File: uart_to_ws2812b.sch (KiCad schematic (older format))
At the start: 27 parts, among them J1 USB_B_Micro, J2 Prog. Header, J3 Power Header, J4 UART, J5 I2C, J6 SPI, J8 Conn_01x03, J9 Conn_01x03, Q1 Q_NPN_BEC, SW1 SW_Push

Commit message: Updated copper pours to avoid short between V_USB and GND
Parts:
- Q1: Mfr Part # (none) -> MMBT3904; Supplier (none) -> LCSC; Supplier Part # (none) -> C181119
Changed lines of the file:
@@
 F 2 "Package_TO_SOT_SMD:SOT-23" H 5450 3700 50  0001 C CNN
 F 3 "~" H 5250 3600 50  0001 C CNN
+F 4 "MMBT3904" H 5250 3600 50  0001 C CNN "Mfr Part #"
+F 5 "LCSC" H 5250 3600 50  0001 C CNN "Supplier"
+F 6 "C181119" H 5250 3600 50  0001 C CNN "Supplier Part #"
 	1    5250 3600
 	1    0    0    -1

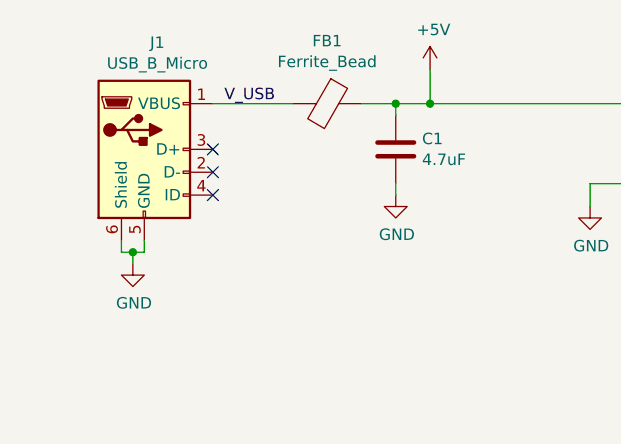
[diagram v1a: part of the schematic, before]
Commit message: Shorted D+ and D- to indicate charging mode
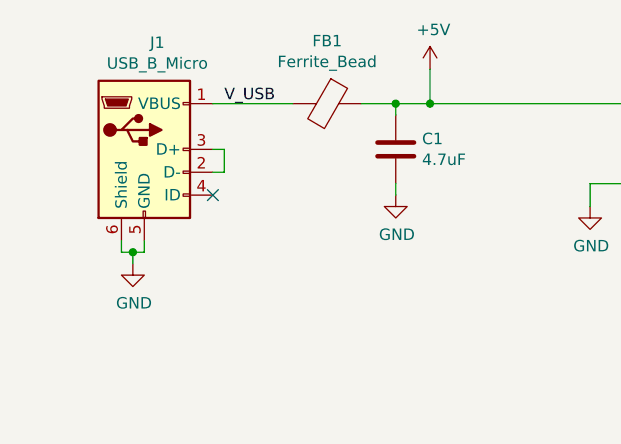
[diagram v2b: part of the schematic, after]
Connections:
- net at J1.2 (D-): now also J1.3 (D+)
- no-connect marks 4 -> 2

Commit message: Changed to a level shifting IC for the LED data logic
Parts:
- removed Q1: Q_NPN_BEC, Package_TO_SOT_SMD:SOT-23, symbol Device:Q_NPN_BEC
- removed R1: 1kR, Resistor_SMD:R_0603_1608Metric, symbol Device:R
- removed R2, R3: 10kR, Resistor_SMD:R_0603_1608Metric, symbol Device:R
- added C2, C22: 0.1uF, Capacitor_SMD:C_0603_1608Metric, symbol Device:C
- added U3: PI4ULS5V201TAEX, Package_TO_SOT_SMD:SOT-23-6, symbol Chinesium:PI4ULS5V201TAEX
- J1: symbol Connector:USB_B_Micro -> uart_to_ws2812b-rescue:USB_B_Micro-Connector
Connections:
- net +3V3: now also C2.1, U3.3 (VCCA), U3.6 (EN)
- net +5V: now also C22.1, U3.4 (VCCB)
- net 3.3V_Data_Out: now also U3.1 (A)
- net 5V_Data_Out: now also U3.5 (B)
- net GND: now also C2.2, C22.2, U3.2 (GND)
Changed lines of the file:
@@
 $EndDescr
 $Comp
-L Connector:USB_B_Micro J1
+L uart_to_ws2812b-rescue:USB_B_Micro-Connector J1
 U 1 1 5F57F340
 P 1900 1550
@@
 Wire Wire Line
 	6850 3200 6850 1850
-Connection ~ 6850 3200
 $Comp
 L power:+3V3 #PWR0104
@@
 	1    0    0    -1
 $EndComp
-Wire Wire Line
-	5650 3200 6850 3200
-Connection ~ 5650 3200
-Wire Wire Line
-	5650 3100 5650 3200
-Wire Wire Line
-	5350 3200 5650 3200
-Wire Wire Line
-	5650 2750 5650 2800
-$Comp
-L power:+5V #PWR0118
-U 1 1 5F5E0732
-P 5650 2750
-F 0 "#PWR0118" H 5650 2600 50  0001 C CNN
-F 1 "+5V" H 5665 2923 50  0000 C CNN
-F 2 "" H 5650 2750 50  0001 C CNN
-F 3 "" H 5650 2750 50  0001 C CNN
-	1    5650 2750
-	1    0    0    -1
-$EndComp
-Text Label 6000 3200 0    50   ~ 0
+Text Label 6850 3200 2    50   ~ 0
 5V_Data_Out
-Text Label 4950 3600 2    50   ~ 0
-Data_B
-Wire Wire Line
-	3500 3600 4350 3600
-Wire Wire Line
-	4850 3150 4850 3200
-$Comp
-L power:+3V3 #PWR0117
-U 1 1 5F5D8C70
-P 4850 3150
-F 0 "#PWR0117" H 4850 3000 50  0001 C CNN
-F 1 "+3V3" H 4865 3323 50  0000 C CNN
-F 2 "" H 4850 3150 50  0001 C CNN
-F 3 "" H 4850 3150 50  0001 C CNN
-	1    4850 3150
-	1    0    0    -1
-$EndComp
-Wire Wire Line
-	4850 3600 5050 3600
-Connection ~ 4850 3600
-Wire Wire Line
-	4850 3500 4850 3600
-Wire Wire Line
-	4650 3600 4850 3600
-Wire Wire Line
-	5350 3400 5350 3200
-$Comp
-L Device:R R3
-U 1 1 5F5D41AD
-P 5650 2950
-F 0 "R3" H 5720 2996 50  0000 L CNN
-F 1 "10kR" H 5720 2905 50  0000 L CNN
-F 2 "Resistor_SMD:R_0603_1608Metric" V 5580 2950 50  0001 C CNN
-F 3 "~" H 5650 2950 50  0001 C CNN
-	1    5650 2950
-	1    0    0    -1
-$EndComp
-Wire Wire Line
-	5350 3900 5350 3800
-$Comp
-L power:GND #PWR0116
-U 1 1 5F5D296A
-P 5350 3900
-F 0 "#PWR0116" H 5350 3650 50  0001 C CNN
-F 1 "GND" H 5355 3727 50  0000 C CNN
-F 2 "" H 5350 3900 50  0001 C CNN
-F 3 "" H 5350 3900 50  0001 C CNN
-	1    5350 3900
-	1    0    0    -1
-$EndComp
-$Comp
-L Device:R R2
-U 1 1 5F5D23C3
-P 4850 3350
-F 0 "R2" H 4920 3396 50  0000 L CNN
-F 1 "10kR" H 4920 3305 50  0000 L CNN
-F 2 "Resistor_SMD:R_0603_1608Metric" V 4780 3350 50  0001 C CNN
-F 3 "~" H 4850 3350 50  0001 C CNN
-	1    4850 3350
-	1    0    0    -1
-$EndComp
-$Comp
-L Device:R R1
-U 1 1 5F5D2061
-P 4500 3600
-F 0 "R1" V 4293 3600 50  0000 C CNN
-F 1 "1kR" V 4384 3600 50  0000 C CNN
-F 2 "Resistor_SMD:R_0603_1608Metric" V 4430 3600 50  0001 C CNN
-F 3 "~" H 4500 3600 50  0001 C CNN
-	1    4500 3600
-	0    1    1    0
-$EndComp
-$Comp
-L Device:Q_NPN_BEC Q1
-U 1 1 5F5D14BE
-P 5250 3600
-F 0 "Q1" H 5441 3646 50  0000 L CNN
-F 1 "Q_NPN_BEC" H 5441 3555 50  0000 L CNN
-F 2 "Package_TO_SOT_SMD:SOT-23" H 5450 3700 50  0001 C CNN
-F 3 "~" H 5250 3600 50  0001 C CNN
-F 4 "MMBT3904" H 5250 3600 50  0001 C CNN "Mfr Part #"
-F 5 "LCSC" H 5250 3600 50  0001 C CNN "Supplier"
-F 6 "C181119" H 5250 3600 50  0001 C CNN "Supplier Part #"
-	1    5250 3600
-	1    0    0    -1
-$EndComp
 Text Label 3650 4900 0    50   ~ 0
 SWCLK
@@
 Wire Wire Line
 	2250 1650 2200 1650
+$Comp
+L Chinesium:PI4ULS5V201TAEX U3
+U 1 1 6003F84C
+P 5300 3650
+F 0 "U3" H 5550 3150 50  0000 R CNN
+F 1 "PI4ULS5V201TAEX" H 5150 3150 50  0000 R CNN
+F 2 "Package_TO_SOT_SMD:SOT-23-6" H 5300 3650 50  0001 C CNN
+F 3 "" H 5300 3650 50  0001 C CNN
+	1    5300 3650
+	1    0    0    -1
+$EndComp
+$Comp
+L power:GND #PWR0116
+U 1 1 60040822
+P 5300 4250
+F 0 "#PWR0116" H 5300 4000 50  0001 C CNN
+F 1 "GND" H 5305 4077 50  0000 C CNN
+F 2 "" H 5300 4250 50  0001 C CNN
+F 3 "" H 5300 4250 50  0001 C CNN
+	1    5300 4250
+	1    0    0    -1
+$EndComp
+Wire Wire Line
+	5300 4250 5300 4150
+Wire Wire Line
+	3500 3600 4900 3600
+$Comp
+L power:+3V3 #PWR0117
+U 1 1 6004D8A9
+P 5900 3850
+F 0 "#PWR0117" H 5900 3700 50  0001 C CNN
+F 1 "+3V3" H 5915 4023 50  0000 C CNN
+F 2 "" H 5900 3850 50  0001 C CNN
+F 3 "" H 5900 3850 50  0001 C CNN
+	1    5900 3850
+	1    0    0    -1
+$EndComp
+Wire Wire Line
+	5700 3800 5700 3900
+Wire Wire Line
+	5700 3900 5900 3900
+Wire Wire Line
+	5900 3900 5900 3850
+$Comp
+L power:+3V3 #PWR0118
+U 1 1 60052295
+P 5200 3000
+F 0 "#PWR0118" H 5200 2850 50  0001 C CNN
+F 1 "+3V3" H 5215 3173 50  0000 C CNN
+F 2 "" H 5200 3000 50  0001 C CNN
+F 3 "" H 5200 3000 50  0001 C CNN
+	1    5200 3000
+	1    0    0    -1
+$EndComp
+Wire Wire Line
+	5200 3000 5200 3150
+$Comp
+L power:+5V #PWR0133
+U 1 1 60055D96
+P 5400 3000
+F 0 "#PWR0133" H 5400 2850 50  0001 C CNN
+F 1 "+5V" H 5415 3173 50  0000 C CNN
+F 2 "" H 5400 3000 50  0001 C CNN
+F 3 "" H 5400 3000 50  0001 C CNN
+	1    5400 3000
+	1    0    0    -1
+$EndComp
+Wire Wire Line
+	5400 3000 5400 3150
+$Comp
+L power:+3V3 #PWR0134
+U 1 1 600598E4
+P 4700 2800
+F 0 "#PWR0134" H 4700 2650 50  0001 C CNN
+F 1 "+3V3" H 4715 2973 50  0000 C CNN
+F 2 "" H 4700 2800 50  0001 C CNN
+F 3 "" H 4700 2800 50  0001 C CNN
+	1    4700 2800
+	1    0    0    -1
+$EndComp
+$Comp
+L Device:C C2
+U 1 1 60059DA7
+P 4700 2950
+F 0 "C2" H 4815 2996 50  0000 L CNN
+F 1 "0.1uF" H 4815 2905 50  0000 L CNN
+F 2 "Capacitor_SMD:C_0603_1608Metric" H 4738 2800 50  0001 C CNN
+F 3 "~" H 4700 2950 50  0001 C CNN
+	1    4700 2950
+	1    0    0    -1
+$EndComp
+$Comp
+L power:GND #PWR0135
+U 1 1 6005A5C0
+P 4700 3100
+F 0 "#PWR0135" H 4700 2850 50  0001 C CNN
+F 1 "GND" H 4705 2927 50  0000 C CNN
+F 2 "" H 4700 3100 50  0001 C CNN
+F 3 "" H 4700 3100 50  0001 C CNN
+	1    4700 3100
+	1    0    0    -1
+$EndComp
+$Comp
+L Device:C C22
+U 1 1 6006167A
+P 5800 2950
+F 0 "C22" H 5915 2996 50  0000 L CNN
+F 1 "0.1uF" H 5915 2905 50  0000 L CNN
+F 2 "Capacitor_SMD:C_0603_1608Metric" H 5838 2800 50  0001 C CNN
+F 3 "~" H 5800 2950 50  0001 C CNN
+	1    5800 2950
+	1    0    0    -1
+$EndComp
+$Comp
+L power:GND #PWR0137
+U 1 1 60061684
+P 5800 3100
+F 0 "#PWR0137" H 5800 2850 50  0001 C CNN
+F 1 "GND" H 5805 2927 50  0000 C CNN
+F 2 "" H 5800 3100 50  0001 C CNN
+F 3 "" H 5800 3100 50  0001 C CNN
+	1    5800 3100
+	1    0    0    -1
+$EndComp
+Wire Wire Line
+	6400 3600 6400 3200
+Wire Wire Line
+	6400 3200 6850 3200
+Wire Wire Line
+	5700 3600 6400 3600
+Connection ~ 6850 3200
+$Comp
+L power:+5V #PWR0136
+U 1 1 6007D6FB
+P 5800 2800
+F 0 "#PWR0136" H 5800 2650 50  0001 C CNN
+F 1 "+5V" H 5815 2973 50  0000 C CNN
+F 2 "" H 5800 2800 50  0001 C CNN
+F 3 "" H 5800 2800 50  0001 C CNN
+	1    5800 2800
+	1    0    0    -1
+$EndComp
 $EndSCHEMATC

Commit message: Updated component information with more detail
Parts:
- C1: Mfr Part # (none) -> CL10A475KQ8NNNC; Supplier (none) -> LCSC; Supplier Part # (none) -> C8032
- U3: Mfr Part # (none) -> PI4ULS5V201TAEX; Supplier (none) -> LCSC; Supplier Part # (none) -> C181736
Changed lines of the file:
@@
 $EndDescr
-$Comp
-L uart_to_ws2812b-rescue:USB_B_Micro-Connector J1
-U 1 1 5F57F340
-P 1900 1550
-F 0 "J1" H 1957 2017 50  0000 C CNN
-F 1 "USB_B_Micro" H 1957 1926 50  0000 C CNN
-F 2 "chinesium:USB-MicroB" H 2050 1500 50  0001 C CNN
-F 3 "~" H 2050 1500 50  0001 C CNN
-	1    1900 1550
-	1    0    0    -1
-$EndComp
-NoConn ~ 2200 1750
-$Comp
-L power:GND #PWR0101
-U 1 1 5F580144
-P 1850 2050
-F 0 "#PWR0101" H 1850 1800 50  0001 C CNN
-F 1 "GND" H 1855 1877 50  0000 C CNN
-F 2 "" H 1850 2050 50  0001 C CNN
-F 3 "" H 1850 2050 50  0001 C CNN
-	1    1850 2050
-	1    0    0    -1
-$EndComp
-Wire Wire Line
-	1800 1950 1800 2000
-Wire Wire Line
-	1800 2000 1850 2000
-Wire Wire Line
-	1900 2000 1900 1950
-Wire Wire Line
-	1850 2000 1850 2050
-Connection ~ 1850 2000
-Wire Wire Line
-	1850 2000 1900 2000
-$Comp
-L power:+5V #PWR0102
-U 1 1 5F580CD5
-P 3150 1200
-F 0 "#PWR0102" H 3150 1050 50  0001 C CNN
-F 1 "+5V" H 3165 1373 50  0000 C CNN
-F 2 "" H 3150 1200 50  0001 C CNN
-F 3 "" H 3150 1200 50  0001 C CNN
-	1    3150 1200
-	1    0    0    -1
-$EndComp
-Text Label 2250 1350 0    50   ~ 0
-V_USB
-$Comp
-L Device:Ferrite_Bead FB1
-U 1 1 5F5816BE
-P 2700 1350
-F 0 "FB1" V 2426 1350 50  0000 C CNN
-F 1 "Ferrite_Bead" V 2517 1350 50  0000 C CNN
-F 2 "Inductor_SMD:L_0805_2012Metric" V 2630 1350 50  0001 C CNN
-F 3 "~" H 2700 1350 50  0001 C CNN
-	1    2700 1350
-	0    1    1    0
-$EndComp
-Wire Wire Line
-	2200 1350 2550 1350
-Wire Wire Line
-	2850 1350 3000 1350
-Wire Wire Line
-	3150 1350 3150 1200
-$Comp
-L Device:C C1
-U 1 1 5F5827DA
-P 3000 1550
-F 0 "C1" H 3115 1596 50  0000 L CNN
-F 1 "4.7uF" H 3115 1505 50  0000 L CNN
-F 2 "Capacitor_SMD:C_0603_1608Metric" H 3038 1400 50  0001 C CNN
-F 3 "~" H 3000 1550 50  0001 C CNN
-	1    3000 1550
-	1    0    0    -1
-$EndComp
-$Comp
-L power:GND #PWR0103
-U 1 1 5F582C49
-P 3000 1750
-F 0 "#PWR0103" H 3000 1500 50  0001 C CNN
-F 1 "GND" H 3005 1577 50  0000 C CNN
-F 2 "" H 3000 1750 50  0001 C CNN
-F 3 "" H 3000 1750 50  0001 C CNN
-	1    3000 1750
-	1    0    0    -1
-$EndComp
-Wire Wire Line
-	3000 1750 3000 1700
-Wire Wire Line
-	3000 1400 3000 1350
-Connection ~ 3000 1350
-Wire Wire Line
-	3000 1350 3150 1350
-$Sheet
-S 4000 1200 750  750
-U 5F588D8C
-F0 "3V3-LDO" 50
-F1 "3V3-LDO.sch" 50
-F2 "VIN" I L 4000 1350 50
-F3 "VOUT" U R 4750 1350 50
-F4 "GND" U L 4000 1700 50
-$EndSheet
-Connection ~ 3150 1350
-$Comp
-L power:GND #PWR0106
-U 1 1 5F58C806
-P 3850 1800
-F 0 "#PWR0106" H 3850 1550 50  0001 C CNN
-F 1 "GND" H 3855 1627 50  0000 C CNN
-F 2 "" H 3850 1800 50  0001 C CNN
-F 3 "" H 3850 1800 50  0001 C CNN
-	1    3850 1800
-	1    0    0    -1
-$EndComp
-Wire Wire Line
-	3850 1800 3850 1700
-Wire Wire Line
-	3850 1700 4000 1700
-$Comp
-L power:+3V3 #PWR0107
-U 1 1 5F58D1E8
-P 4900 1250
-F 0 "#PWR0107" H 4900 1100 50  0001 C CNN
-F 1 "+3V3" H 4915 1423 50  0000 C CNN
-F 2 "" H 4900 1250 50  0001 C CNN
-F 3 "" H 4900 1250 50  0001 C CNN
-	1    4900 1250
-	1    0    0    -1
-$EndComp
-Wire Wire Line
-	4900 1250 4900 1350
-Wire Wire Line
-	4900 1350 4750 1350
 $Comp
 L Connector_Generic:Conn_02x03_Odd_Even J2
@@
 	1    0    0    -1
 $EndComp
-Wire Wire Line
-	3150 1350 4000 1350
 Wire Wire Line
 	6850 3200 6850 1850
@@
 F17 "SWCLK" T R 3500 4900 50
 $EndSheet
-Wire Wire Line
-	2200 1550 2250 1550
-Wire Wire Line
-	2250 1550 2250 1650
-Wire Wire Line
-	2250 1650 2200 1650
 $Comp
 L Chinesium:PI4ULS5V201TAEX U3
@@
 F 1 "PI4ULS5V201TAEX" H 5150 3150 50  0000 R CNN
 F 2 "Package_TO_SOT_SMD:SOT-23-6" H 5300 3650 50  0001 C CNN
-F 3 "" H 5300 3650 50  0001 C CNN
+F 3 "https://datasheet.lcsc.com/szlcsc/1811082050_Diodes-Incorporated-PI4ULS5V201TAEX_C181736.pdf" H 5300 3650 50  0001 C CNN
+F 4 "PI4ULS5V201TAEX" H 5300 3650 50  0001 C CNN "Mfr Part #"
+F 5 "LCSC" H 5300 3650 50  0001 C CNN "Supplier"
+F 6 "C181736" H 5300 3650 50  0001 C CNN "Supplier Part #"
 	1    5300 3650
 	1    0    0    -1
@@
 	1    0    0    -1
 $EndComp
+$Comp
+L uart_to_ws2812b-rescue:USB_B_Micro-Connector J1
+U 1 1 5F57F340
+P 1900 1550
+F 0 "J1" H 1957 2017 50  0000 C CNN
+F 1 "USB_B_Micro" H 1957 1926 50  0000 C CNN
+F 2 "chinesium:USB-MicroB" H 2050 1500 50  0001 C CNN
+F 3 "~" H 2050 1500 50  0001 C CNN
+	1    1900 1550
+	1    0    0    -1
+$EndComp
+NoConn ~ 2200 1750
+$Comp
+L power:GND #PWR0101
+U 1 1 5F580144
+P 1850 2050
+F 0 "#PWR0101" H 1850 1800 50  0001 C CNN
+F 1 "GND" H 1855 1877 50  0000 C CNN
+F 2 "" H 1850 2050 50  0001 C CNN
+F 3 "" H 1850 2050 50  0001 C CNN
+	1    1850 2050
+	1    0    0    -1
+$EndComp
+Wire Wire Line
+	1800 1950 1800 2000
+Wire Wire Line
+	1800 2000 1850 2000
+Connection ~ 1850 2000
+Wire Wire Line
+	1900 2000 1900 1950
+Wire Wire Line
+	1850 2000 1850 2050
+Wire Wire Line
+	1850 2000 1900 2000
+Text Label 2250 1350 0    50   ~ 0
+V_USB
+$Comp
+L Device:Ferrite_Bead FB1
+U 1 1 5F5816BE
+P 2700 1350
+F 0 "FB1" V 2426 1350 50  0000 C CNN
+F 1 "Ferrite_Bead" V 2517 1350 50  0000 C CNN
+F 2 "Inductor_SMD:L_0805_2012Metric" V 2630 1350 50  0001 C CNN
+F 3 "~" H 2700 1350 50  0001 C CNN
+	1    2700 1350
+	0    1    1    0
+$EndComp
+Wire Wire Line
+	2200 1350 2550 1350
+Wire Wire Line
+	2200 1550 2250 1550
+Wire Wire Line
+	2250 1550 2250 1650
+Wire Wire Line
+	2250 1650 2200 1650
+Wire Wire Line
+	2850 1350 3000 1350
+Wire Wire Line
+	3150 1350 4000 1350
+Wire Wire Line
+	4900 1350 4750 1350
+Wire Wire Line
+	4900 1250 4900 1350
+$Comp
+L power:+3V3 #PWR0107
+U 1 1 5F58D1E8
+P 4900 1250
+F 0 "#PWR0107" H 4900 1100 50  0001 C CNN
+F 1 "+3V3" H 4915 1423 50  0000 C CNN
+F 2 "" H 4900 1250 50  0001 C CNN
+F 3 "" H 4900 1250 50  0001 C CNN
+	1    4900 1250
+	1    0    0    -1
+$EndComp
+Wire Wire Line
+	3850 1700 4000 1700
+Wire Wire Line
+	3850 1800 3850 1700
+$Comp
+L power:GND #PWR0106
+U 1 1 5F58C806
+P 3850 1800
+F 0 "#PWR0106" H 3850 1550 50  0001 C CNN
+F 1 "GND" H 3855 1627 50  0000 C CNN
+F 2 "" H 3850 1800 50  0001 C CNN
+F 3 "" H 3850 1800 50  0001 C CNN
+	1    3850 1800
+	1    0    0    -1
+$EndComp
+Connection ~ 3150 1350
+$Sheet
+S 4000 1200 750  750
+U 5F588D8C
+F0 "3V3-LDO" 50
+F1 "3V3-LDO.sch" 50
+F2 "VIN" I L 4000 1350 50
+F3 "VOUT" U R 4750 1350 50
+F4 "GND" U L 4000 1700 50
+$EndSheet
+Wire Wire Line
+	3000 1350 3150 1350
+Connection ~ 3000 1350
+Wire Wire Line
+	3000 1400 3000 1350
+Wire Wire Line
+	3000 1750 3000 1700
+$Comp
+L power:GND #PWR0103
+U 1 1 5F582C49
+P 3000 1750
+F 0 "#PWR0103" H 3000 1500 50  0001 C CNN
+F 1 "GND" H 3005 1577 50  0000 C CNN
+F 2 "" H 3000 1750 50  0001 C CNN
+F 3 "" H 3000 1750 50  0001 C CNN
+	1    3000 1750
+	1    0    0    -1
+$EndComp
+$Comp
+L Device:C C1
+U 1 1 5F5827DA
+P 3000 1550
+F 0 "C1" H 3115 1596 50  0000 L CNN
+F 1 "4.7uF" H 3115 1505 50  0000 L CNN
+F 2 "Capacitor_SMD:C_0603_1608Metric" H 3038 1400 50  0001 C CNN
+F 3 "https://datasheet.lcsc.com/szlcsc/1811151136_Samsung-Electro-Mechanics-CL10A475KQ8NNNC_C8032.pdf" H 3000 1550 50  0001 C CNN
+F 4 "CL10A475KQ8NNNC" H 3000 1550 50  0001 C CNN "Mfr Part #"
+F 5 "LCSC" H 3000 1550 50  0001 C CNN "Supplier"
+F 6 "C8032" H 3000 1550 50  0001 C CNN "Supplier Part #"
+	1    3000 1550
+	1    0    0    -1
+$EndComp
+Wire Wire Line
+	3150 1350 3150 1200
+$Comp
+L power:+5V #PWR0102
+U 1 1 5F580CD5
+P 3150 1200
+F 0 "#PWR0102" H 3150 1050 50  0001 C CNN
+F 1 "+5V" H 3165 1373 50  0000 C CNN
+F 2 "" H 3150 1200 50  0001 C CNN
+F 3 "" H 3150 1200 50  0001 C CNN
+	1    3150 1200
+	1    0    0    -1
+$EndComp
